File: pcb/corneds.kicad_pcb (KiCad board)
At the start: 2 copper layers, 320 x 104.9 mm, 120 parts, among them J3 AudioJack4, J4 AudioJack4, SW1 SW_Push, SW10 SW_Push, SW11 SW_Push, SW12 SW_Push, SW13 SW_Push, SW14 SW_Push, SW15 SW_Push, SW16 SW_Push, SW17 SW_Push, SW18 SW_Push, SW19 SW_Push, SW2 SW_Push, SW20 SW_Push, SW21 SW_Push, SW22 SW_Push, SW23 SW_Push, SW24 SW_Push, SW25 SW_Push, SW26 SW_Push, SW27 SW_Push, SW28 SW_Push, SW29 SW_Push, SW3 SW_Push, SW30 SW_Push, SW31 SW_Push, SW32 SW_Push, SW33 SW_Push, SW34 SW_Push, SW35 SW_Push, SW36 SW_Push, SW37 SW_Push, SW38 SW_Push, SW39 SW_Push, SW4 SW_Push, SW40 SW_Push, SW41 SW_Push, SW42 SW_Push, SW5 SW_Push, SW6 SW_Push, SW7 SW_Push, SW8 SW_Push, SW9 SW_Push, U1 Pico, U2 Pico, U3 SWD_Connector_3pin, U4 SWD_Connector_3pin, U5 Debug_UART_l, U6 Debug_UART_r

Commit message: fixed trrs jacks and via shapes
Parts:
- J3, J4: moved to B.Cu
- moved J3 8.20 mm to (123.8, 101.4)
- moved J4 7.89 mm to (165.4, 95.9)
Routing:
- net /vcc_l: track 223.3 -> 234.1 mm, vias 0 -> 1
- net /xboard_uart_rx_r: track 93.8 -> 103.3 mm
- net /xboard_uart_tx_l: track 117.9 -> 114.7 mm
- net /vcc_r: track 240.4 -> 237.6 mm

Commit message: routed left side, placed 3 more mounting holes but want one more
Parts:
- J3, J4: footprint Connector_Audio:Jack_3.5mm_PJ320E_Horizontal -> entropy:Jack_3.5mm_boardsource_TRRS_TH
- moved U5 56.5 mm to (14.0, 50.1), turned to 33 degrees
- moved U6 55.9 mm to (277.7, 50.1), turned to -33 degrees
- moved GP2 43.6 mm to (238.8, 110.5)
- moved GP1 43.6 mm to (50.8, 110.5)
- moved TP8 33.6 mm to (243.8, 110.5)
- moved TP1 33.6 mm to (45.7, 110.5)
- moved D10 19.1 mm to (266.0, 74.0)
- moved D11 19.1 mm to (266.0, 93.0)
- moved D12 19.1 mm to (266.0, 112.0)
- moved D7 19.1 mm to (8.44, 74.0)
- moved D8 19.1 mm to (8.44, 93.0)
- moved D9 19.1 mm to (8.44, 112.0)
- moved SW10 19.1 mm to (273.6, 69.2)
- moved SW11 19.1 mm to (273.6, 88.2)
- moved SW12 19.1 mm to (273.6, 107.2)
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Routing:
- net /vcc_r: track 237.6 -> 0.00 mm, vias 1 -> 0
- net /col0_r: track 224.9 -> 0.00 mm
- net /col1_r: track 204.1 -> 0.00 mm, vias 3 -> 0
- net /col3_r: track 202.2 -> 0.00 mm, vias 5 -> 0
- net /col4_r: track 199.6 -> 0.00 mm, vias 5 -> 0
- net /col5_r: track 199.3 -> 0.00 mm, vias 4 -> 0
- net /dbg_uart_tx_r: track 192.4 -> 0.00 mm, vias 1 -> 0
- net /dbg_uart_rx_r: track 191.3 -> 0.00 mm, vias 1 -> 0
- net /col2_r: track 179.2 -> 0.00 mm, vias 3 -> 0
- net /row0_r: track 173.4 -> 0.00 mm, vias 1 -> 0
- net /row2_r: track 173.2 -> 0.00 mm, vias 2 -> 0
- net /row1_r: track 170.9 -> 0.00 mm, vias 3 -> 0
- net /row3_r: track 151.8 -> 0.00 mm, vias 2 -> 0
- net /xboard_uart_rx_r: track 103.3 -> 0.00 mm
- net /xboard_uart_tx_r: track 95.6 -> 0.00 mm, vias 1 -> 0
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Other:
- board size 320 x 104.9 mm -> 320 x 105.6 mm

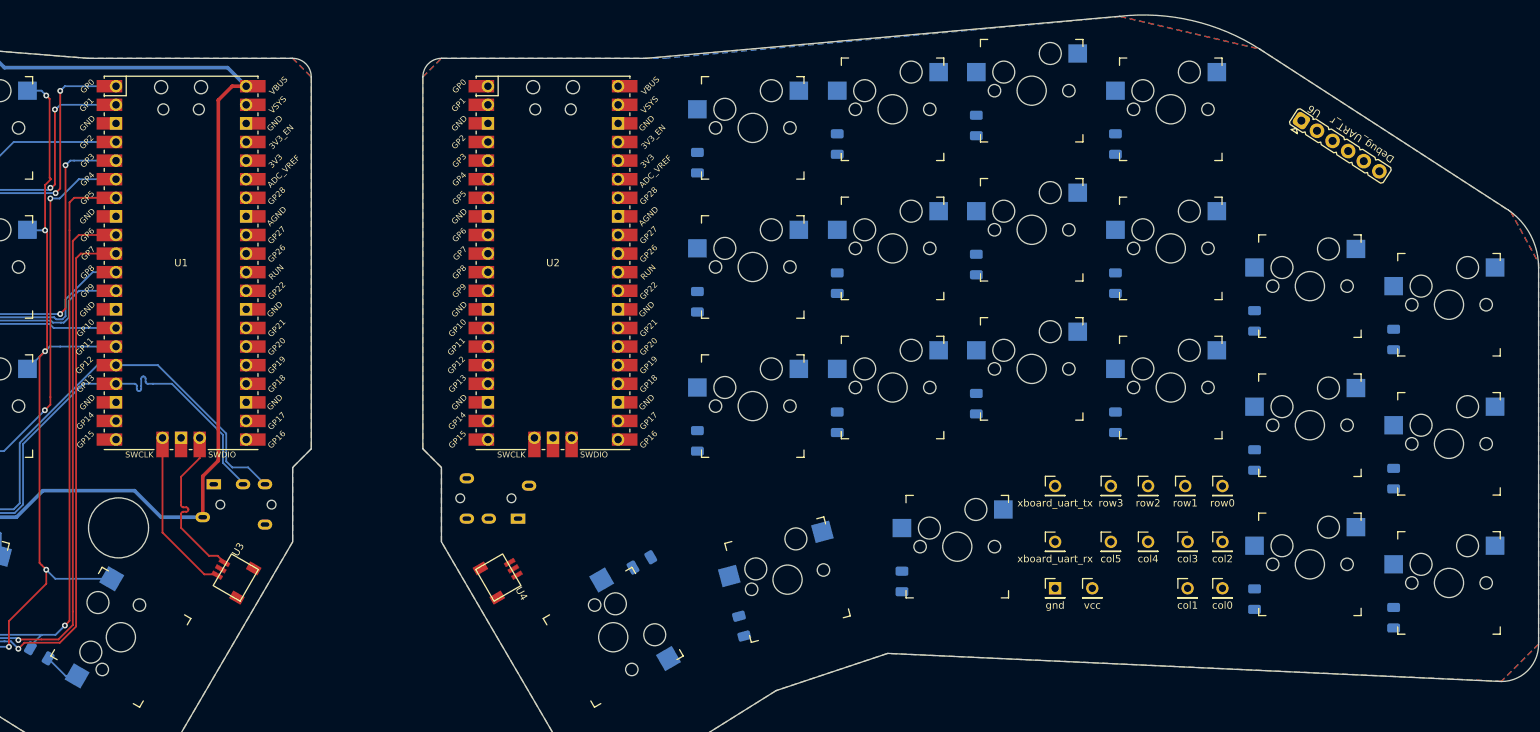
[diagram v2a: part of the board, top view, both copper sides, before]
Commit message: finished layout on both sides and design front and back plates
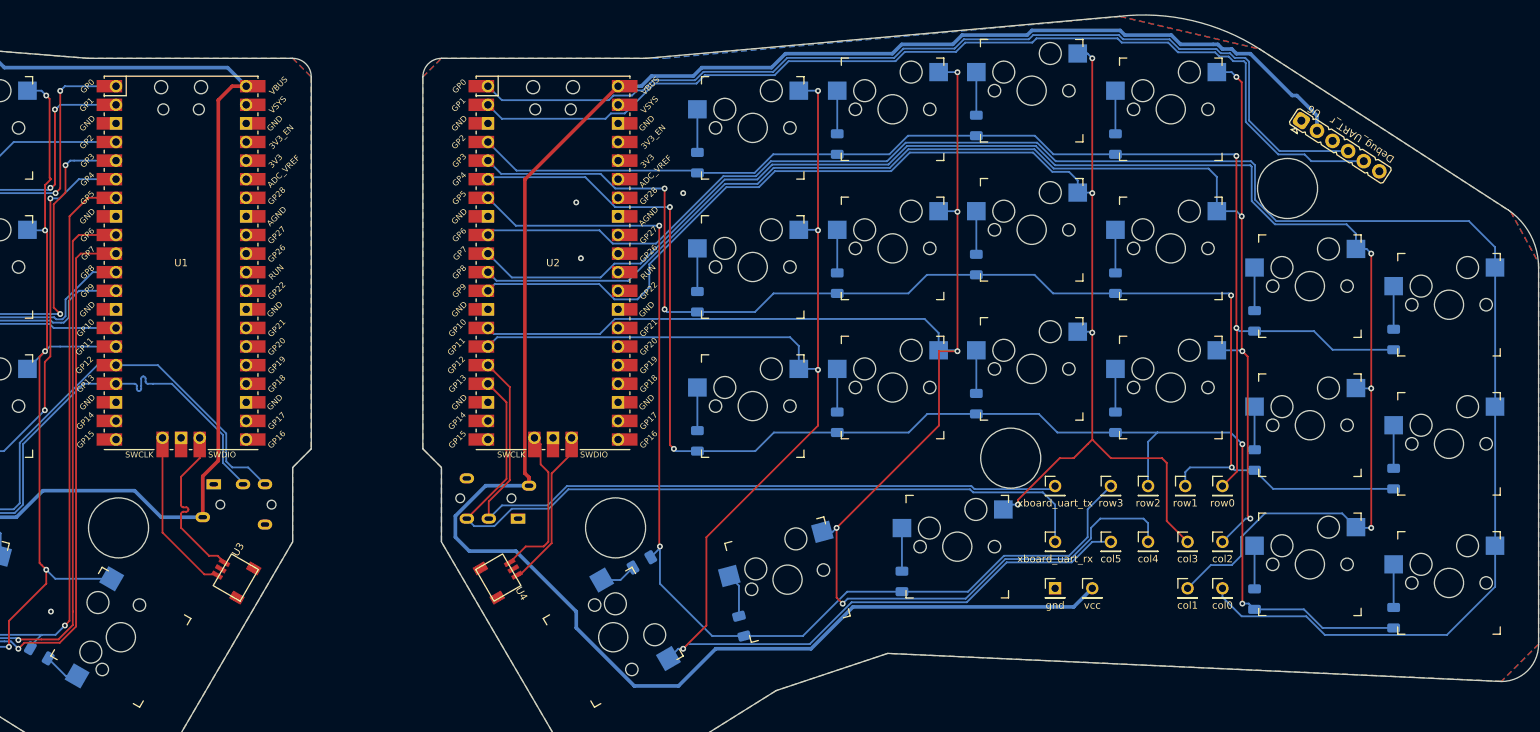
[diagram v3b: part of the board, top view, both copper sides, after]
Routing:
- net /vcc_r: track 0.00 -> 282.5 mm
- net /col0_r: track 0.00 -> 242.7 mm
- net /col1_r: track 0.00 -> 210.7 mm, vias 0 -> 3
- net /col4_r: track 0.00 -> 207.3 mm, vias 0 -> 5
- net /col5_r: track 0.00 -> 205.4 mm, vias 0 -> 4
- net /col3_r: track 0.00 -> 193.6 mm, vias 0 -> 4
- net /row2_r: track 0.00 -> 193.1 mm, vias 0 -> 4
- net /col2_r: track 0.00 -> 190.2 mm, vias 0 -> 4
- net /row1_r: track 0.00 -> 178.4 mm, vias 0 -> 4
- net /row0_r: track 0.00 -> 175.9 mm, vias 0 -> 2
- net /row3_r: track 0.00 -> 151.2 mm, vias 0 -> 2
- net /dbg_uart_rx_r: track 0.00 -> 136.6 mm
- net /dbg_uart_tx_r: track 0.00 -> 133.2 mm
- net /xboard_uart_rx_r: track 0.00 -> 110.5 mm
- net /xboard_uart_tx_r: track 0.00 -> 102.9 mm
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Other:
- outline, holes or cut-outs redrawn

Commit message: updated date in silk
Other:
- board text added: "26 Apr 2023"
- board text removed: "23 Mar 2023"
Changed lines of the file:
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@@
     (effects (font (size 1.5 1.5) (thickness 0.3)) (justify mirror))
   )
-  (gr_text "23 Mar 2023" (at 179.578 130.81) (layer "B.SilkS")
+  (gr_text "26 Apr 2023" (at 179.578 130.81) (layer "B.SilkS")
     (effects (font (size 1.5 1.5) (thickness 0.3)) (justify mirror))
   )
-  (gr_text "23 Mar 2023" (at 109.982 131.064) (layer "B.SilkS")
+  (gr_text "26 Apr 2023" (at 109.982 131.064) (layer "B.SilkS")
     (effects (font (size 1.5 1.5) (thickness 0.3)) (justify mirror))
   )
